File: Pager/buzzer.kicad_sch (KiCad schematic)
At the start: 1 part, among them Q1 AO3400A

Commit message: br
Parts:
- added BZ1: Buzzer, Package_DFN_QFN:Texas_RVA_VQFN-16-1EP_3.5x3.5mm_P0.5mm_EP2.14x2.14mm_ThermalVias, symbol Device:Buzzer
- added D2: D_Small, symbol Device:D_Small
- added R19: 100, Resistor_THT:R_Array_SIP4, symbol Device:R_Small
- added R20: R_Small, Resistor_THT:R_Array_SIP4, symbol Device:R_Small
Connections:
- net at Q1.1 (G): now also R19.1, R20.1
- net GND: now reaches Q1.2 (S)
- net GND: now also R20.2
- net at Q1.3 (D): now also BZ1.2 (-), D2.2 (A)
- new net BUZZER_PWM: R19.2
- new net V_{BATT}: BZ1.1 (+), D2.1 (K)
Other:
- moved on the sheet: Q1

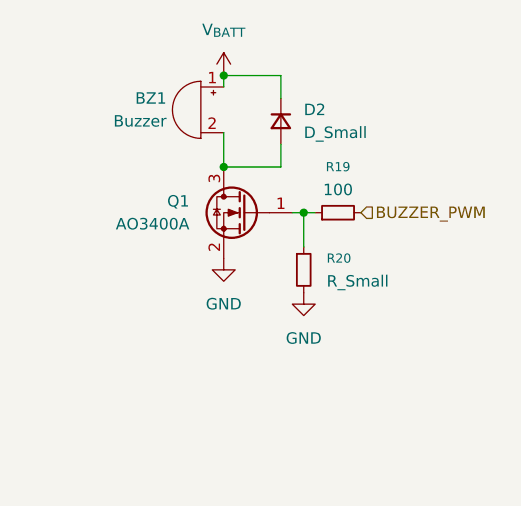
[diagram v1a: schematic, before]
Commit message: Schematic Review, Footprints Added, Need Screen
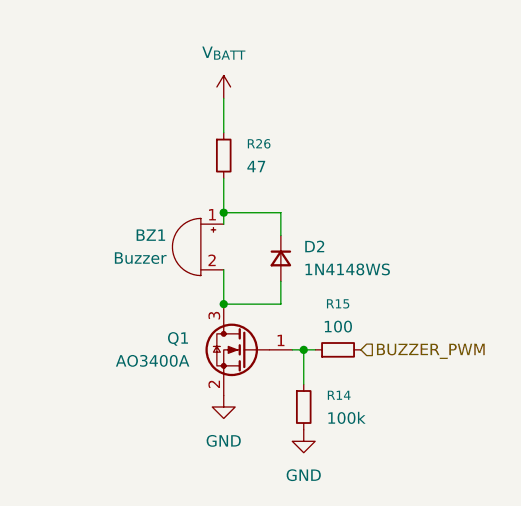
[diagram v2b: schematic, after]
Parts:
- added R26: 47, Resistor_SMD:R_0805_2012Metric, symbol Device:R_Small
- BZ1: footprint Package_DFN_QFN:Texas_RVA_VQFN-16-1EP_3.5x3.5mm_P0.5mm_EP2.14x2.14mm_ThermalVias -> Buzzer:XDCR_AT-1220-TT-R
- D2: value D_Small -> 1N4148WS; footprint (none) -> Diode_SMD:D_SOD-323
- R14: renamed from R20; value R_Small -> 100k; footprint Resistor_THT:R_Array_SIP4 -> Resistor_SMD:R_0603_1608Metric
- R15: renamed from R19; footprint Resistor_THT:R_Array_SIP4 -> Resistor_SMD:R_0603_1608Metric
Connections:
- net V_{BATT}: now also R26.1; no longer BZ1.1 (+), D2.1 (K)
- new net: BZ1.1 (+), D2.1 (K), R26.2
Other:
- moved on the sheet: BZ1, D2, Q1, R14, R15

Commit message: layout
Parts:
- R14, R15: footprint Resistor_SMD:R_0603_1608Metric -> Resistor_SMD:R_0805_2012Metric_Pad1.20x1.40mm_HandSolder
- R26: footprint Resistor_SMD:R_0805_2012Metric -> Resistor_SMD:R_0805_2012Metric_Pad1.20x1.40mm_HandSolder
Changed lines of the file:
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@@
 			)
 		)
-		(property "Footprint" "Resistor_SMD:R_0805_2012Metric"
+		(property "Footprint" "Resistor_SMD:R_0805_2012Metric_Pad1.20x1.40mm_HandSolder"
 			(at 59.69 29.21 0)
 			(hide yes)
@@
 			)
 		)
-		(property "Footprint" "Resistor_SMD:R_0603_1608Metric"
+		(property "Footprint" "Resistor_SMD:R_0805_2012Metric_Pad1.20x1.40mm_HandSolder"
 			(at 68.58 57.15 0)
 			(hide yes)
@@
 			)
 		)
-		(property "Footprint" "Resistor_SMD:R_0603_1608Metric"
+		(property "Footprint" "Resistor_SMD:R_0805_2012Metric_Pad1.20x1.40mm_HandSolder"
 			(at 72.39 50.8 0)
 			(hide yes)
